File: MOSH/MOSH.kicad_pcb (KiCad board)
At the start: 2 copper layers, 68.6 x 62.2 mm, 25 parts, among them J1 Power, J2 Digital/PWM, J3 Analog, J4 Digital/PWM, J5 Conn_01x08_Socket, J6 Conn_01x03_Pin, Q1 IRF540N, U1 LTC1050, U2 MCP41100

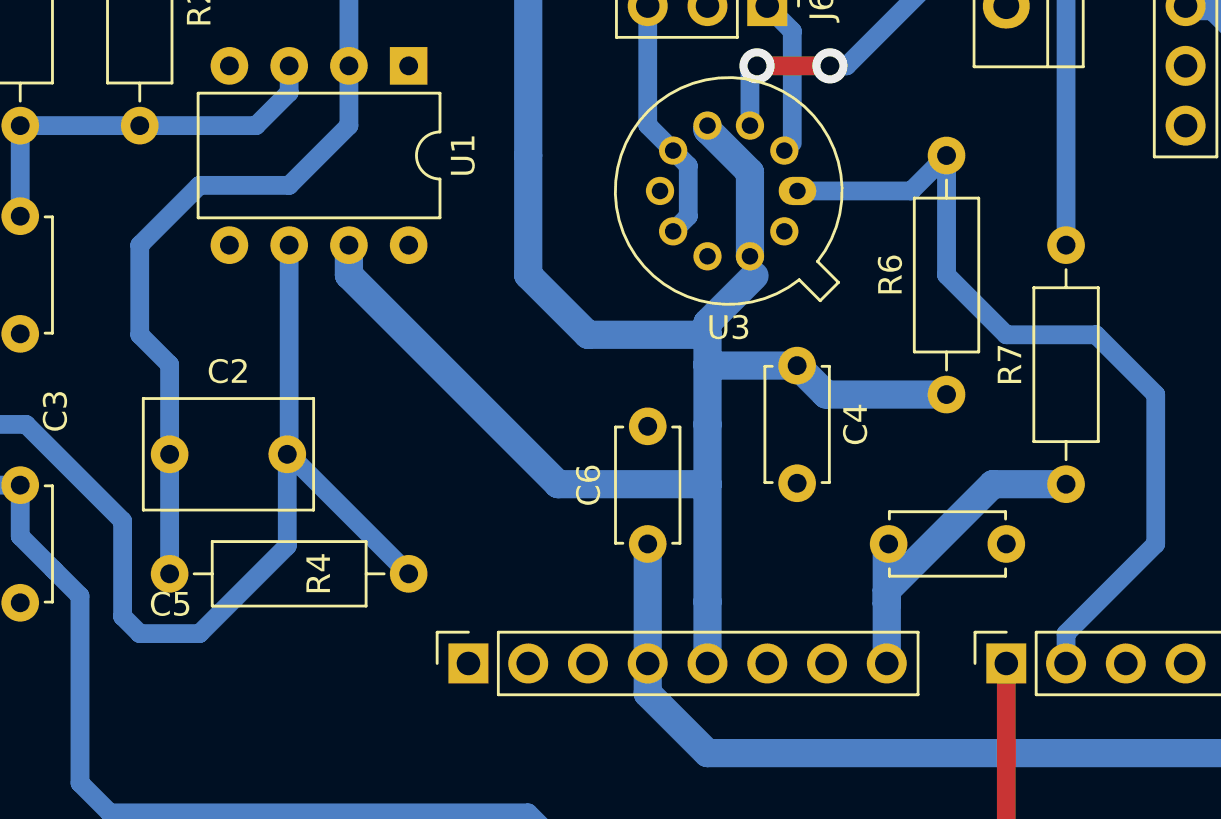
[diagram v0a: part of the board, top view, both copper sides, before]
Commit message: run design rules check and correct some things
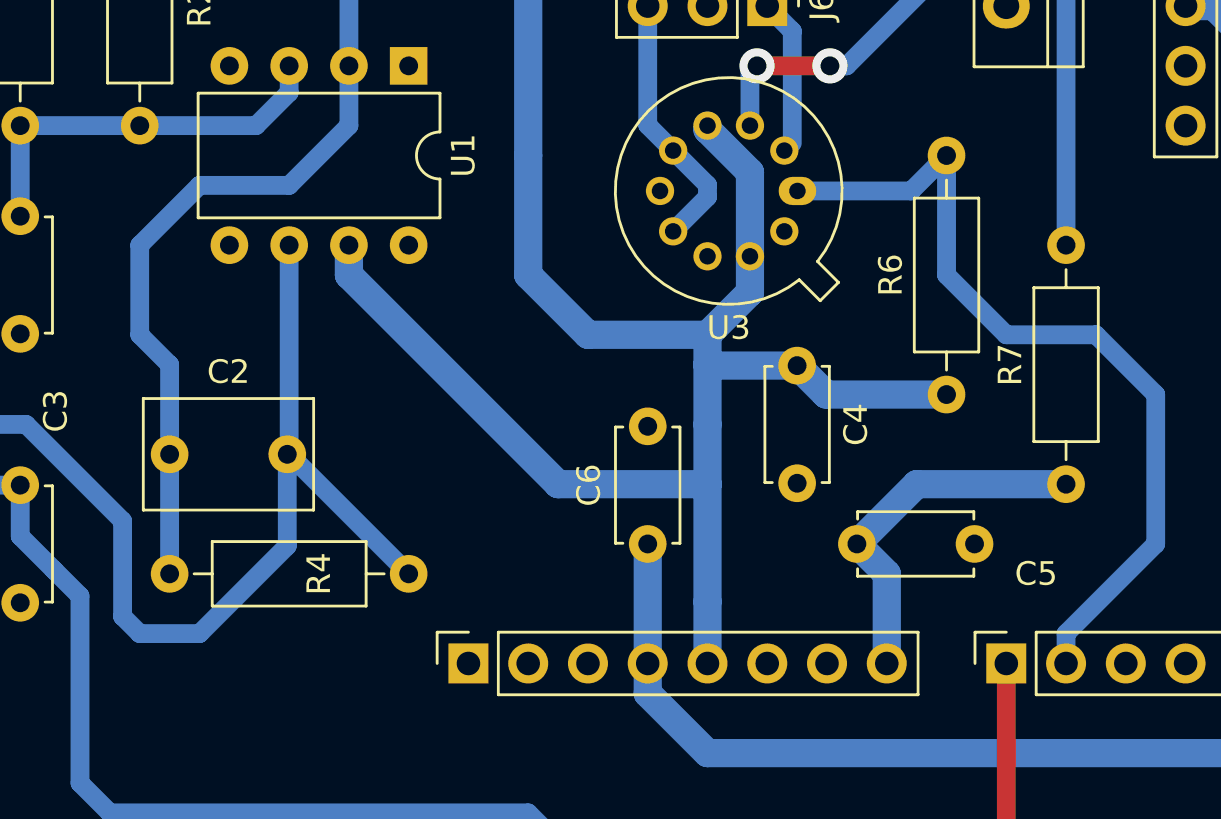
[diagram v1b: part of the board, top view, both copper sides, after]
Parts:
- moved C5 1.35 mm to (144.4, 92.4)
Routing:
- net +5V: track 79.7 -> 80.4 mm
- net ISENS2: track 10.6 -> 11.2 mm
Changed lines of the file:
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@@
   )
   (footprint "Capacitor_THT:C_Disc_D4.7mm_W2.5mm_P5.00mm" placed (layer "F.Cu")
-    (at 145.8 92.38)
+    (at 144.45 92.38)
     (descr "C, Disc series, Radial, pin pitch=5.00mm, , diameter*width=4.7*2.5mm^2, Capacitor, http://www.vishay.com/docs/45233/krseries.pdf")
     (tags "C Disc series Radial pin pitch 5.00mm  diameter 4.7mm width 2.5mm Capacitor")
@@
     (property "ki_keywords" "cap capacitor")
     (attr through_hole)
-    (fp_text reference "C5" (at -30.52 2.58) (layer "F.SilkS")
+    (fp_text reference "C5" (at 7.62 1.27) (layer "F.SilkS")
         (effects (font (size 1 1) (thickness 0.15)))
     )
@@
   (segment (start 138.1 87.3) (end 138.1 84.76) (width 1.2) (layer "B.Cu") (net 3))
   (segment (start 133.02 83.49) (end 138.1 83.49) (width 1.2) (layer "B.Cu") (net 3))
+  (segment (start 139.90466 81.68534) (end 139.90466 80.15417) (width 1.2) (layer "B.Cu") (net 3))
   (segment (start 139.90466 76.579899) (end 139.90466 80.15417) (width 1.2) (layer "B.Cu") (net 3))
   (segment (start 143.14 86.03) (end 141.91 84.8) (width 1.2) (layer "B.Cu") (net 3))
@@
   (segment (start 131.75 89.84) (end 138.1 89.84) (width 1.2) (layer "B.Cu") (net 3))
   (segment (start 138.14 84.8) (end 138.1 84.76) (width 1.2) (layer "B.Cu") (net 3))
-  (segment (start 138.1 83.49) (end 138.1 82.982598) (width 1.2) (layer "B.Cu") (net 3))
   (segment (start 138.1 89.84) (end 138.1 87.3) (width 1.2) (layer "B.Cu") (net 3))
   (segment (start 138.1 74.775239) (end 139.90466 76.579899) (width 1.2) (layer "B.Cu") (net 3))
   (segment (start 138.1 84.76) (end 138.1 83.49) (width 1.2) (layer "B.Cu") (net 3))
+  (segment (start 138.1 83.49) (end 139.90466 81.68534) (width 1.2) (layer "B.Cu") (net 3))
   (segment (start 122.86 79.68) (end 122.86 80.95) (width 1.2) (layer "B.Cu") (net 3))
   (segment (start 141.91 84.8) (end 138.14 84.8) (width 1.2) (layer "B.Cu") (net 3))
@@
   (segment (start 130.48 64.44) (end 130.48 75.87) (width 1.2) (layer "B.Cu") (net 3))
   (segment (start 130.48 75.87) (end 130.48 80.95) (width 1.2) (layer "B.Cu") (net 3))
-  (segment (start 138.1 82.982598) (end 140.1 80.982598) (width 1.2) (layer "B.Cu") (net 3))
   (segment (start 158.42 69.52) (end 159.622081 69.52) (width 1.2) (layer "B.Cu") (net 5))
   (segment (start 164.77 92.38) (end 167.905 95.515) (width 1.2) (layer "B.Cu") (net 5))
@@
   (segment (start 158.42 59.36) (end 156.86 59.36) (width 0.8) (layer "B.Cu") (net 24))
   (segment (start 158.42 49.2) (end 158.42 56.82) (width 0.8) (layer "B.Cu") (net 26))
-  (segment (start 145.72 97.46) (end 145.72 94.92) (width 1.2) (layer "B.Cu") (net 27))
-  (segment (start 145.72 94.92) (end 145.72 92.46) (width 1.2) (layer "B.Cu") (net 27))
-  (segment (start 150.22873 89.84) (end 145.72 94.34873) (width 1.2) (layer "B.Cu") (net 27))
-  (segment (start 145.72 94.34873) (end 145.72 94.92) (width 1.2) (layer "B.Cu") (net 27))
-  (segment (start 153.34 89.84) (end 150.22873 89.84) (width 1.2) (layer "B.Cu") (net 27))
+  (segment (start 145.72 93.65) (end 144.45 92.38) (width 1.2) (layer "B.Cu") (net 27))
+  (segment (start 146.99 89.84) (end 144.45 92.38) (width 1.2) (layer "B.Cu") (net 27))
+  (segment (start 145.72 97.46) (end 145.72 93.65) (width 1.2) (layer "B.Cu") (net 27))
+  (segment (start 153.34 89.84) (end 146.99 89.84) (width 1.2) (layer "B.Cu") (net 27))
   (segment (start 140.64 69.52) (end 141.70466 70.58466) (width 0.8) (layer "B.Cu") (net 32))
   (segment (start 141.70466 70.58466) (end 141.70466 75.345585) (width 0.8) (layer "B.Cu") (net 32))
@@
   (segment (start 108.89 64.44) (end 108.89 61.9) (width 0.8) (layer "B.Cu") (net 33))
   (segment (start 134.29 60.63) (end 138.1 64.44) (width 0.8) (layer "B.Cu") (net 33))
+  (segment (start 138.1 77.120752) (end 138.1 77.633418) (width 0.8) (layer "B.Cu") (net 34))
   (segment (start 135.56 74.580752) (end 136.64 75.660752) (width 0.8) (layer "B.Cu") (net 34))
-  (segment (start 136.64 75.660752) (end 137.28233 76.303082) (width 0.8) (layer "B.Cu") (net 34))
+  (segment (start 138.1 77.633418) (end 136.64 79.093418) (width 0.8) (layer "B.Cu") (net 34))
   (segment (start 135.56 69.52) (end 135.56 74.580752) (width 0.8) (layer "B.Cu") (net 34))
-  (segment (start 137.28233 76.303082) (end 137.28233 78.451088) (width 0.8) (layer "B.Cu") (net 34))
-  (segment (start 137.28233 78.451088) (end 136.64 79.093418) (width 0.8) (layer "B.Cu") (net 34))
+  (segment (start 136.64 75.660752) (end 138.1 77.120752) (width 0.8) (layer "B.Cu") (net 34))
   (segment (start 150.8 64.44) (end 145.72 64.44) (width 0.8) (layer "B.Cu") (net 35))
   (segment (start 143.30466 72.06) (end 140.20516 72.06) (width 0.8) (layer "F.Cu") (net 36))

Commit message: add title
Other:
- board text added: "ISS 2023 AJB & RM Gas Sensor"
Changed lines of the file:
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@@
   (paper "A4")
   (title_block
+    (title "ISS 2023 AJB & RM - Gas Sensor")
     (date "mar. 31 mars 2015")
   )
@@
   (gr_line (start 100 45.39) (end 168.58 45.39)
     (stroke (width 0.15) (type solid)) (layer "Edge.Cuts"))
+  (gr_text "ISS 2023 AJB & RM\nGas Sensor" (at 100 56.82) (layer "F.Cu")
+    (effects (font (size 1.5 1.5) (thickness 0.3) bold) (justify left bottom))
+  )
   (gr_text "ICSP" (at 164.897 72.06 90) (layer "Dwgs.User")
     (effects (font (size 1 1) (thickness 0.15)))
